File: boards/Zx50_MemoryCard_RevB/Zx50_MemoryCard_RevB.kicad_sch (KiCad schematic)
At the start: 43 parts, among them J1 3.3V, J2 Zx50_EdgeConnector, J3 TP_CLK, J4 TP_MCLK, J5 GND, J6 GND, J7 GND, SW1 SW_DIP_x05, U1 AMS1117-3.3, U10 74LVC245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

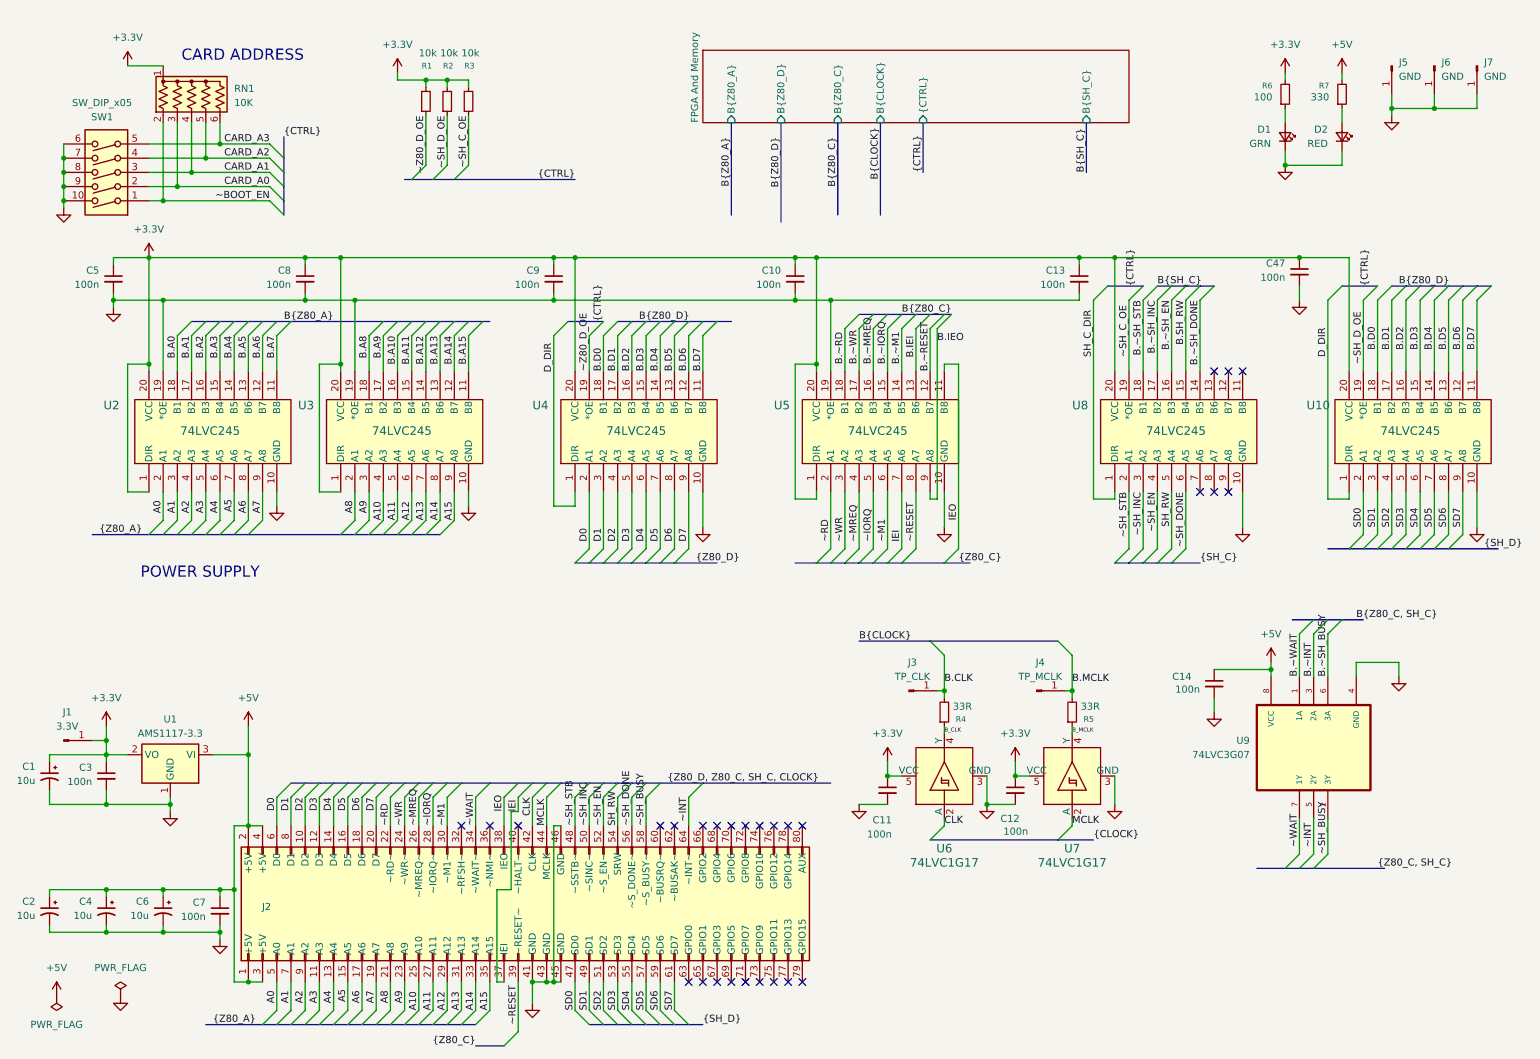
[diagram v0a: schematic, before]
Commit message: fixup pic z80 timing.  add memory test script to pico
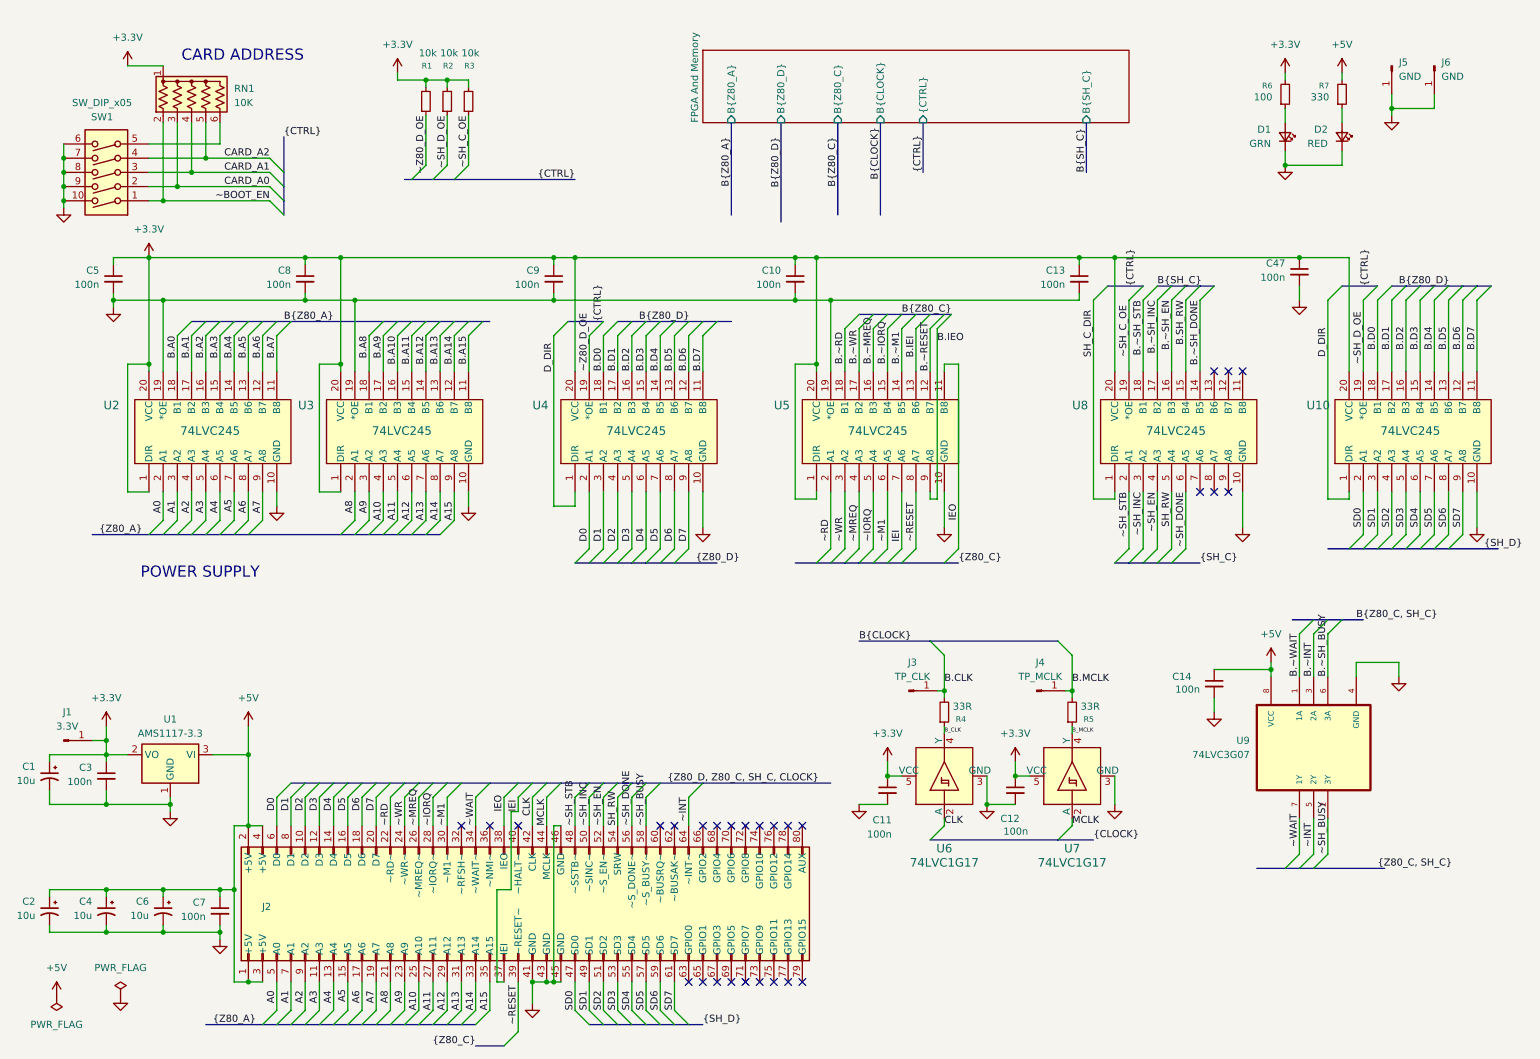
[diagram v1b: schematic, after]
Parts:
- removed J7: GND, Connector_PinHeader_2.54mm:PinHeader_1x01_P2.54mm_Vertical, symbol Connector:Conn_01x01_Pin
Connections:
- net CARD_A3: no longer names the net of RN1.6 (R5), SW1.5
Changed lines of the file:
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@@
 	(bus_alias "CTRL"
 		(members "D_DIR" "~Z80_D_OE" "~SH_D_OE" "~SH_C_OE" "SH_C_DIR" "RESET" "~BOOT_EN"
-			"CARD_A[0..3]"
+			"CARD_A[0..2]"
 		)
 	)
@@
 	)
 	(junction
-		(at 48.26 34.29)
-		(diameter 0)
-		(color 0 0 0 0)
-	)
-	(junction
 		(at 157.48 62.23)
 		(diameter 0)
@@
 	)
 	(junction
-		(at 265.43 27.94)
-		(diameter 0)
-		(color 0 0 0 0)
-	)
-	(junction
 		(at 20.32 36.83)
 		(diameter 0)
@@
 	)
 	(bus_entry
-		(at 59.69 36.83)
-		(size -2.54 -2.54)
-		(stroke
-			(width 0)
-			(type default)
-		)
-	)
-	(bus_entry
 		(at 72.39 104.14)
 		(size 2.54 -2.54)
@@
 	(wire
 		(pts
-			(xy 273.05 25.4) (xy 273.05 27.94)
-		)
-		(stroke
-			(width 0)
-			(type default)
-		)
-	)
-	(wire
-		(pts
 			(xy 208.28 54.61) (xy 201.93 54.61)
 		)
@@
 		)
 	)
-	(wire
-		(pts
-			(xy 48.26 34.29) (xy 57.15 34.29)
-		)
-		(stroke
-			(width 0)
-			(type default)
-		)
-	)
 	(bus
 		(pts
@@
 	(bus
 		(pts
+			(xy 177.8 109.22) (xy 180.34 109.22)
+		)
+		(stroke
+			(width 0)
+			(type default)
+		)
+	)
+	(bus
+		(pts
 			(xy 45.72 66.04) (xy 48.26 66.04)
 		)
@@
 		)
 	)
-	(wire
-		(pts
-			(xy 48.26 30.48) (xy 48.26 34.29)
-		)
-		(stroke
-			(width 0)
-			(type default)
-		)
-	)
 	(bus
 		(pts
@@
 	(wire
 		(pts
-			(xy 35.56 34.29) (xy 48.26 34.29)
-		)
-		(stroke
-			(width 0)
-			(type default)
-		)
-	)
-	(wire
-		(pts
 			(xy 45.72 96.52) (xy 45.72 101.6)
 		)
@@
 	(bus
 		(pts
-			(xy 59.69 39.37) (xy 59.69 36.83)
-		)
-		(stroke
-			(width 0)
-			(type default)
-		)
-	)
-	(bus
-		(pts
 			(xy 76.2 148.59) (xy 78.74 148.59)
 		)
@@
 	(wire
 		(pts
+			(xy 35.56 34.29) (xy 48.26 34.29)
+		)
+		(stroke
+			(width 0)
+			(type default)
+		)
+	)
+	(wire
+		(pts
 			(xy 151.13 54.61) (xy 151.13 55.88)
 		)
@@
 	(bus
 		(pts
-			(xy 59.69 36.83) (xy 59.69 33.02)
+			(xy 59.69 33.02) (xy 59.69 39.37)
 		)
 		(stroke
@@
 	(wire
 		(pts
-			(xy 63.5 54.61) (xy 69.85 54.61)
+			(xy 48.26 30.48) (xy 48.26 34.29)
 		)
 		(stroke
@@
 		)
 	)
-	(bus
+	(wire
 		(pts
-			(xy 177.8 109.22) (xy 182.372 109.22)
+			(xy 63.5 54.61) (xy 69.85 54.61)
 		)
 		(stroke
@@
 	(wire
 		(pts
-			(xy 273.05 27.94) (xy 265.43 27.94)
-		)
-		(stroke
-			(width 0)
-			(type default)
-		)
-	)
-	(wire
-		(pts
 			(xy 101.6 153.67) (xy 100.33 153.67)
 		)
@@
 		)
 	)
-	(label "CARD_A3"
-		(at 57.15 34.29 180)
-		(effects
-			(font
-				(size 1.27 1.27)
-			)
-			(justify right bottom)
-		)
-	)
 	(label "A3"
 		(at 45.72 100.33 90)
@@
 					(unit 1)
 				)
-			)
-		)
-	)
-	(symbol
-		(lib_id "Connector:Conn_01x01_Pin")
-		(at 273.05 20.32 270)
-		(unit 1)
-		(exclude_from_sim no)
-		(in_bom yes)
-		(on_board yes)
-		(dnp no)
-		(fields_autoplaced yes)
-		(property "Reference" "J7"
-			(at 274.32 19.6849 90)
-			(effects
-				(font
-					(size 1.27 1.27)
-				)
-				(justify left)
-			)
-		)
-		(property "Value" "GND"
-			(at 274.32 22.2249 90)
-			(effects
-				(font
-					(size 1.27 1.27)
-				)
-				(justify left)
-			)
-		)
-		(property "Footprint" "Connector_PinHeader_2.54mm:PinHeader_1x01_P2.54mm_Vertical"
-			(at 273.05 20.32 0)
-			(effects
-				(font
-					(size 1.27 1.27)
-				)
-				(hide yes)
-			)
-		)
-		(property "Datasheet" "~"
-			(at 273.05 20.32 0)
-			(effects
-				(font
-					(size 1.27 1.27)
-				)
-				(hide yes)
-			)
-		)
-		(property "Description" "Generic connector, single row, 01x01, script generated"
-			(at 273.05 20.32 0)
-			(effects
-				(font
-					(size 1.27 1.27)
-				)
-				(hide yes)
-			)
-		)
-		(pin "1"
-		)
-		(instances
-			(project "Zx50_MemoryCard_RevB"
-				(path "/024a2433-248f-41c0-8a0c-ac9ea528ccd5"
-					(reference "J7")
-					(unit 1)
-				)
